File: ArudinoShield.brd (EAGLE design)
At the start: 53.3 x 61.9 mm, 21 parts, among them IC1 L298

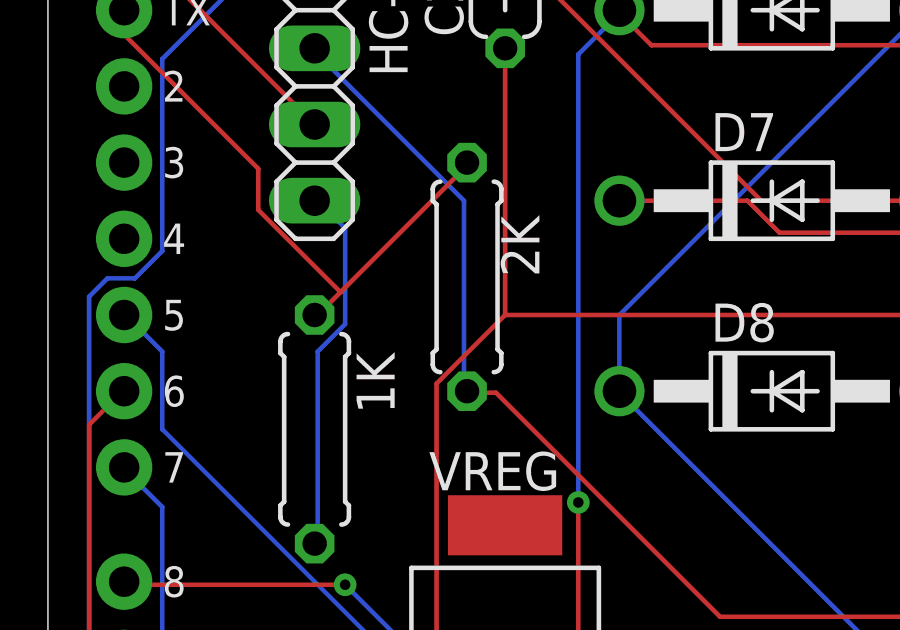
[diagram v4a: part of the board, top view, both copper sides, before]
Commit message: added values, updated gitignore for eagle files
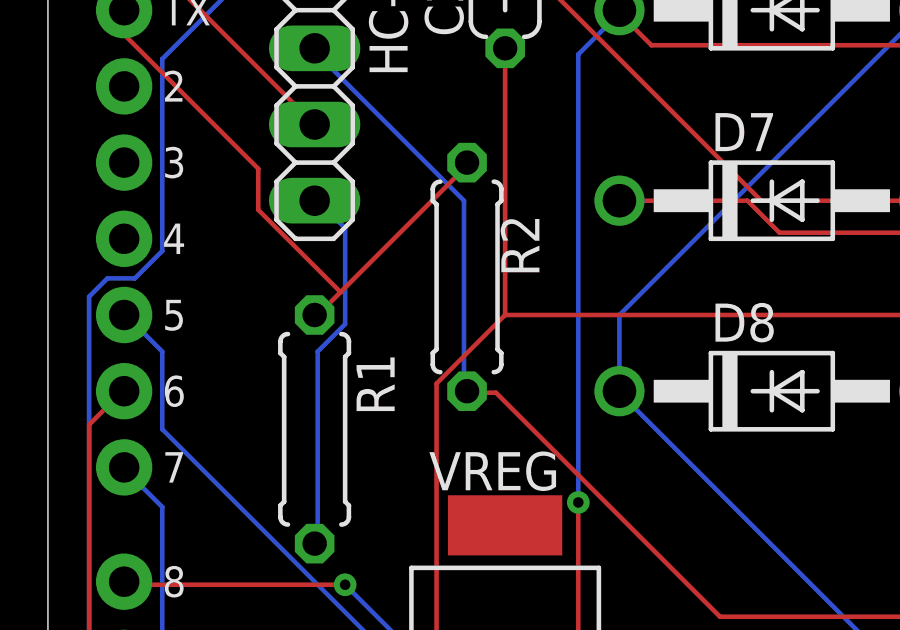
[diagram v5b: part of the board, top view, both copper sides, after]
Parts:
- C1, C2: value (none) -> 220uF/35V
- R1, R3: value (none) -> 1k
- R2: value (none) -> 2K
- renumbered 1K to R1, 2K to R2
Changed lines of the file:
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@@
 <attribute name="VALUE" x="40.005" y="73.66" size="1.27" layer="27" rot="R270"/>
 </element>
-<element name="1K" library="adafruit" package="0207/7" value="" x="43.18" y="57.15" smashed="yes" rot="R270">
+<element name="R1" library="adafruit" package="0207/7" value="1k" x="43.18" y="57.15" smashed="yes" rot="R270">
 <attribute name="NAME" x="44.577" y="59.69" size="1.27" layer="25" ratio="10" rot="R270"/>
 <attribute name="VALUE" x="42.6212" y="59.436" size="1.27" layer="27" ratio="10" rot="R270"/>
 </element>
-<element name="2K" library="adafruit" package="0207/7" value="" x="48.26" y="62.23" smashed="yes" rot="R90">
+<element name="R2" library="adafruit" package="0207/7" value="2K" x="48.26" y="62.23" smashed="yes" rot="R90">
 <attribute name="NAME" x="50.673" y="62.23" size="1.27" layer="25" ratio="10" rot="R90"/>
 <attribute name="VALUE" x="48.8188" y="59.944" size="1.27" layer="27" ratio="10" rot="R90"/>
@@
 <attribute name="VALUE" x="75.3031" y="28.5448" size="1.27" layer="27"/>
 </element>
-<element name="C1" library="rcl" library_urn="urn:adsk.eagle:library:334" package="C050-024X044" package3d_urn="urn:adsk.eagle:package:23643/1" value="" x="38.1" y="24.13" smashed="yes" rot="R90">
+<element name="C1" library="rcl" library_urn="urn:adsk.eagle:library:334" package="C050-024X044" package3d_urn="urn:adsk.eagle:package:23643/1" value="220uF/35V" x="38.1" y="24.13" smashed="yes" rot="R90">
 <attribute name="NAME" x="36.703" y="21.971" size="1.27" layer="25" ratio="10" rot="R90"/>
 <attribute name="POPULARITY" value="14" x="76.2" y="-34.29" size="1.778" layer="27" rot="R90" display="off"/>
@@
 <attribute name="VALUE" x="40.767" y="21.971" size="1.27" layer="27" ratio="10" rot="R90"/>
 </element>
-<element name="C2" library="rcl" library_urn="urn:adsk.eagle:library:334" package="C050-024X044" package3d_urn="urn:adsk.eagle:package:23643/1" value="" x="49.53" y="72.39" smashed="yes" rot="R90">
+<element name="C2" library="rcl" library_urn="urn:adsk.eagle:library:334" package="C050-024X044" package3d_urn="urn:adsk.eagle:package:23643/1" value="220uF/35V" x="49.53" y="72.39" smashed="yes" rot="R90">
 <attribute name="NAME" x="48.133" y="70.231" size="1.27" layer="25" ratio="10" rot="R90"/>
 <attribute name="POPULARITY" value="14" x="92.71" y="6.35" size="1.778" layer="27" rot="R90" display="off"/>
@@
 <attribute name="VALUE" x="52.197" y="70.231" size="1.27" layer="27" ratio="10" rot="R90"/>
 </element>
-<element name="R3" library="rcl" library_urn="urn:adsk.eagle:library:334" package="0207/10" package3d_urn="urn:adsk.eagle:package:23491/2" value="" x="43.18" y="44.45" smashed="yes" rot="R90">
+<element name="R3" library="rcl" library_urn="urn:adsk.eagle:library:334" package="0207/10" package3d_urn="urn:adsk.eagle:package:23491/2" value="1k" x="43.18" y="44.45" smashed="yes" rot="R90">
 <attribute name="NAME" x="41.656" y="41.402" size="1.27" layer="25" ratio="10" rot="R90"/>
 <attribute name="POPULARITY" value="36" x="91.44" y="-1.27" size="1.778" layer="27" rot="R90" display="off"/>
@@
 <contactref element="HC-05" pad="2"/>
 <contactref element="B1" pad="GND@0"/>
-<contactref element="2K" pad="1"/>
+<contactref element="R2" pad="1"/>
 <wire x1="48.1584" y1="64.77" x2="48.1584" y2="58.5216" width="0.1524" layer="16"/>
 <wire x1="43.1292" y1="69.7992" x2="48.1584" y2="64.77" width="0.1524" layer="16"/>
@@
 </signal>
 <signal name="N$11">
-<contactref element="1K" pad="1"/>
+<contactref element="R1" pad="1"/>
 <contactref element="B1" pad="TX"/>
-<contactref element="2K" pad="2"/>
+<contactref element="R2" pad="2"/>
 <wire x1="48.3108" y1="65.9892" x2="44.0436" y2="61.722" width="0.1524" layer="1"/>
 <wire x1="44.0436" y1="61.722" x2="43.2816" y2="60.96" width="0.1524" layer="1"/>
@@
 </signal>
 <signal name="N$14">
-<contactref element="1K" pad="2"/>
+<contactref element="R1" pad="2"/>
 <contactref element="HC-05" pad="4"/>
 <wire x1="43.2816" y1="59.7408" x2="43.2816" y2="53.34" width="0.1524" layer="16"/>

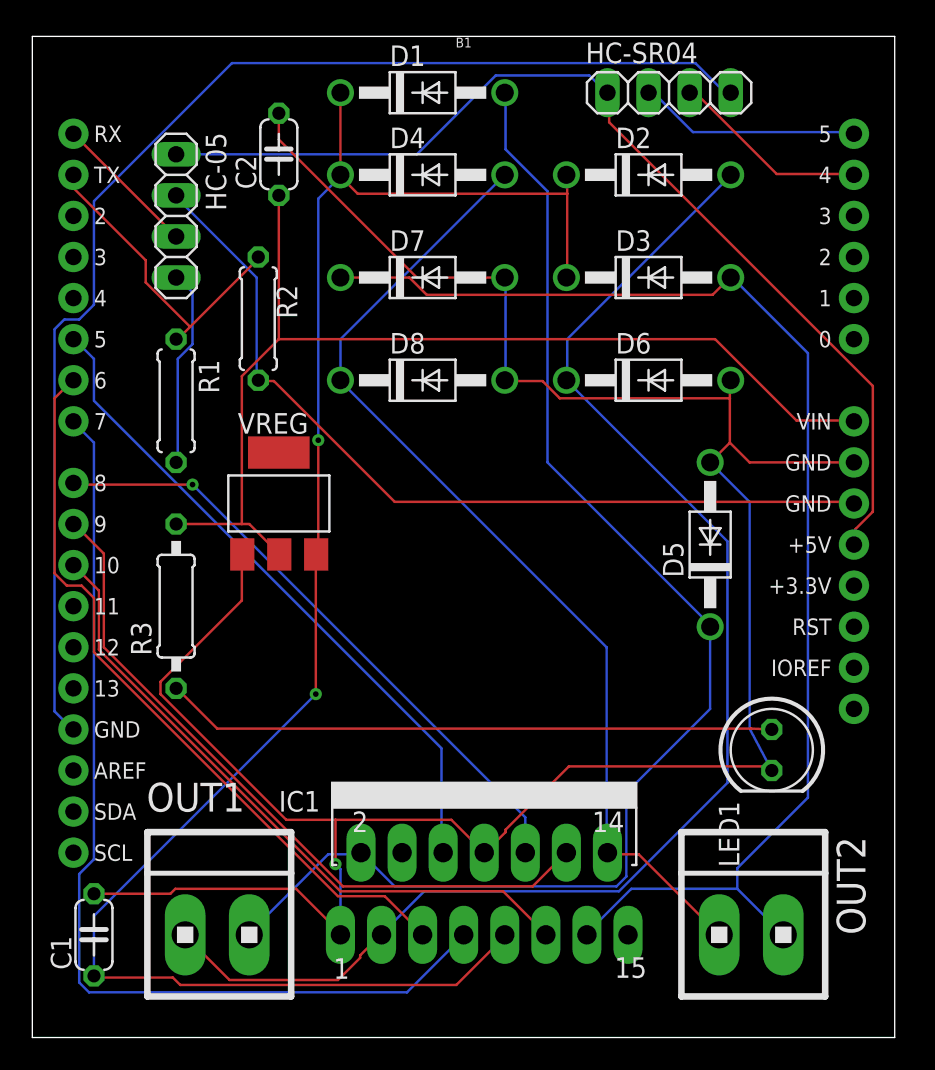
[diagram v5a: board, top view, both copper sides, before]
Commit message: updated schematic for proper pinout from L298 and added supply voltage terminal block
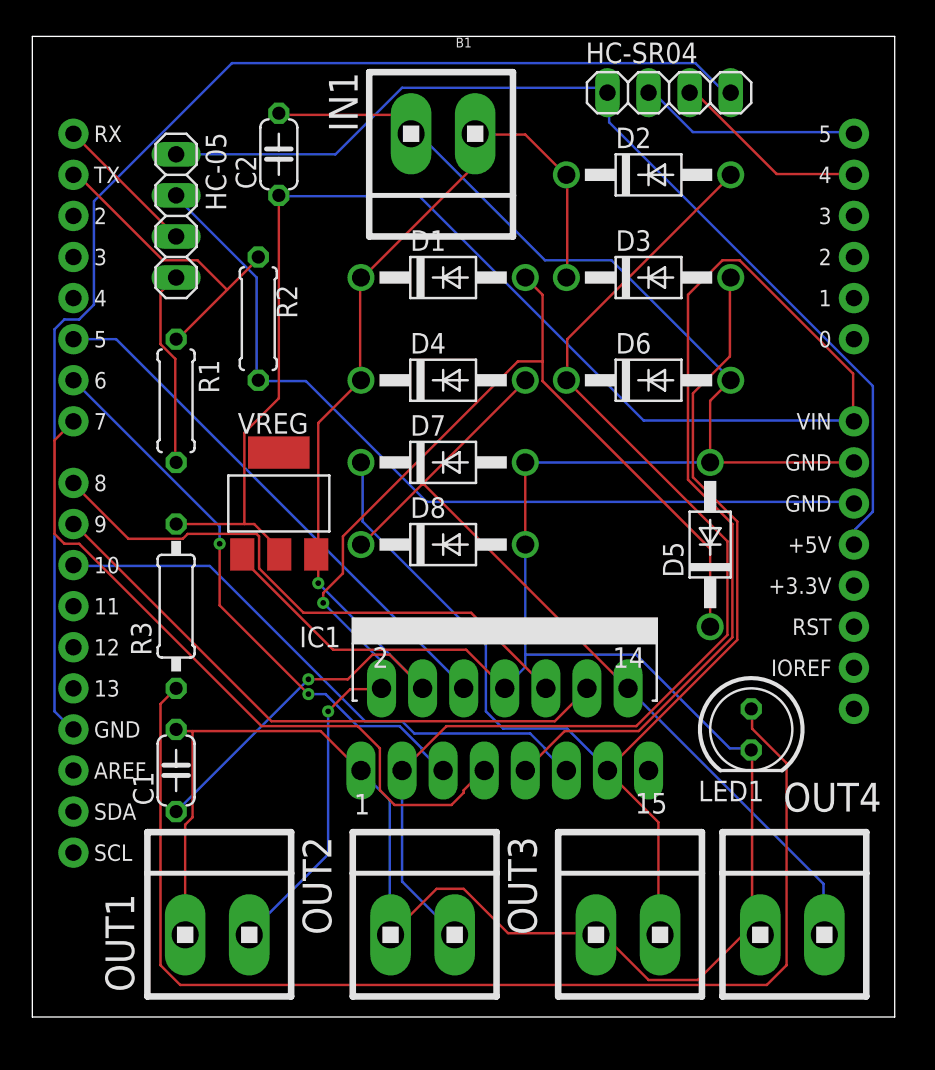
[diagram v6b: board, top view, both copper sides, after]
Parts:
- added IN1, OUT3, OUT4: (no value), con-amp:1X2MTA
- moved OUT2 20.3 mm to (58.4, 24.1)
- moved D4 12.8 mm to (59.7, 58.4)
- moved D1 11.5 mm to (59.7, 64.8)
- moved D7 11.5 mm to (59.7, 53.3)
- moved C1 11.4 mm to (43.2, 34.3)
- moved D8 10.2 mm to (59.7, 48.3)
- moved IC1 10.2 mm to (63.5, 41.9)
- moved LED1 1.80 mm to (78.7, 36.8)
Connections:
- removed net VS: IC1.4
- net N$16: now also OUT2.1; no longer OUT1.2
- net N$17: now also OUT3.1; no longer OUT2.1
- net N$18: now also OUT4.1; no longer OUT2.2
- net N$26: now also IC1.9
- net N$29: now also IN1.1, OUT1.2, OUT2.2, OUT3.2, OUT4.2
- net N$31: now also IC1.4, IN1.2; no longer IC1.9
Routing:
- net N$26: track 66.1 -> 125.4 mm
- net N$25: track 37.9 -> 74.0 mm
- net N$29: track 152.9 -> 187.4 mm, vias 1 -> 0
- net N$31: track 109.0 -> 74.5 mm
- net N$22: track 61.1 -> 43.4 mm
- net N$16: track 85.8 -> 71.8 mm
- net N$21: track 46.4 -> 35.8 mm, vias 0 -> 2
- net N$18: track 62.0 -> 52.6 mm
- net N$15: track 82.5 -> 74.3 mm, vias 0 -> 2
- net N$1: track 41.3 -> 33.1 mm
- net N$24: track 44.0 -> 37.7 mm
- net N$17: track 81.2 -> 75.4 mm
- net N$20: track 40.8 -> 35.8 mm
- net N$2: track 38.7 -> 35.9 mm, vias 1 -> 0
- net N$10: track 64.4 -> 63.8 mm
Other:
- board size 53.3 x 61.9 mm -> 53.3 x 60.6 mm

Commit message: updated schematic and board
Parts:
- added 9G: (no value), pinhead:1X03
- moved R1 11.4 mm to (43.2, 45.7)
- moved HC-05 10.2 mm to (43.2, 58.4)
- moved R3 8.98 mm to (49.5, 38.1)
- moved C1 1.27 mm to (43.2, 35.6)
- renumbered IN1 to VIN
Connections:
- net N$1 renamed ENA
- net N$15 renamed OUT1
- net N$16 renamed OUT2
- net N$17 renamed OUT3
- net N$18 renamed OUT4
- net N$2 renamed IN3
- net N$20 renamed ENB
- net N$21 renamed IN1
- net N$22 renamed IN2
- net N$24 renamed IN4
- net N$31 renamed VIN
- net N$7 renamed ECHO
- net N$8 renamed TRIG
- removed net N$26: B1.VIN, C2.1, IC1.9, R3.2, VREG.2
- removed net N$29: B1.GND@1, C1.2, C2.2, D5.A, D6.A, D7.A, D8.A, IC1.1, IC1.8, LED1.K, OUT1.2, OUT2.2, OUT3.2, OUT4.2, VIN.1, VREG.1
- removed net N$9: B1.GND@2, HC-SR04.4
- new net +5V: 9G.2, B1.VIN, C2.1, IC1.9, R3.2, VREG.2
- new net 9GPWM: 9G.1, B1.D11
- new net GND: 9G.3, B1.GND@1, C1.2, C2.2, D5.A, D6.A, D7.A, D8.A, HC-SR04.4, IC1.1, IC1.15, IC1.8, LED1.K, OUT1.2, OUT2.2, OUT3.2, OUT4.2, VIN.1, VREG.1
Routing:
- net GND: track 0.00 -> 215.0 mm
- net N$29: track 187.4 -> 0.00 mm
- net N$26: track 125.4 -> 0.00 mm
- net +5V: track 0.00 -> 109.1 mm, vias 0 -> 1
- net N$9: track 78.4 -> 0.00 mm
- net N$25: track 74.0 -> 31.3 mm
- net 9GPWM: track 0.00 -> 26.8 mm
- net ENB: track 35.8 -> 60.3 mm
- net IN2: track 43.4 -> 67.8 mm
- net OUT3: track 75.4 -> 98.1 mm
- net N$11: track 19.8 -> 37.9 mm
- net ENA: track 33.1 -> 50.3 mm
- net IN4: track 37.7 -> 54.6 mm, vias 0 -> 1
- net N$12: track 8.98 -> 19.2 mm
- net IN1: track 35.8 -> 44.0 mm
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
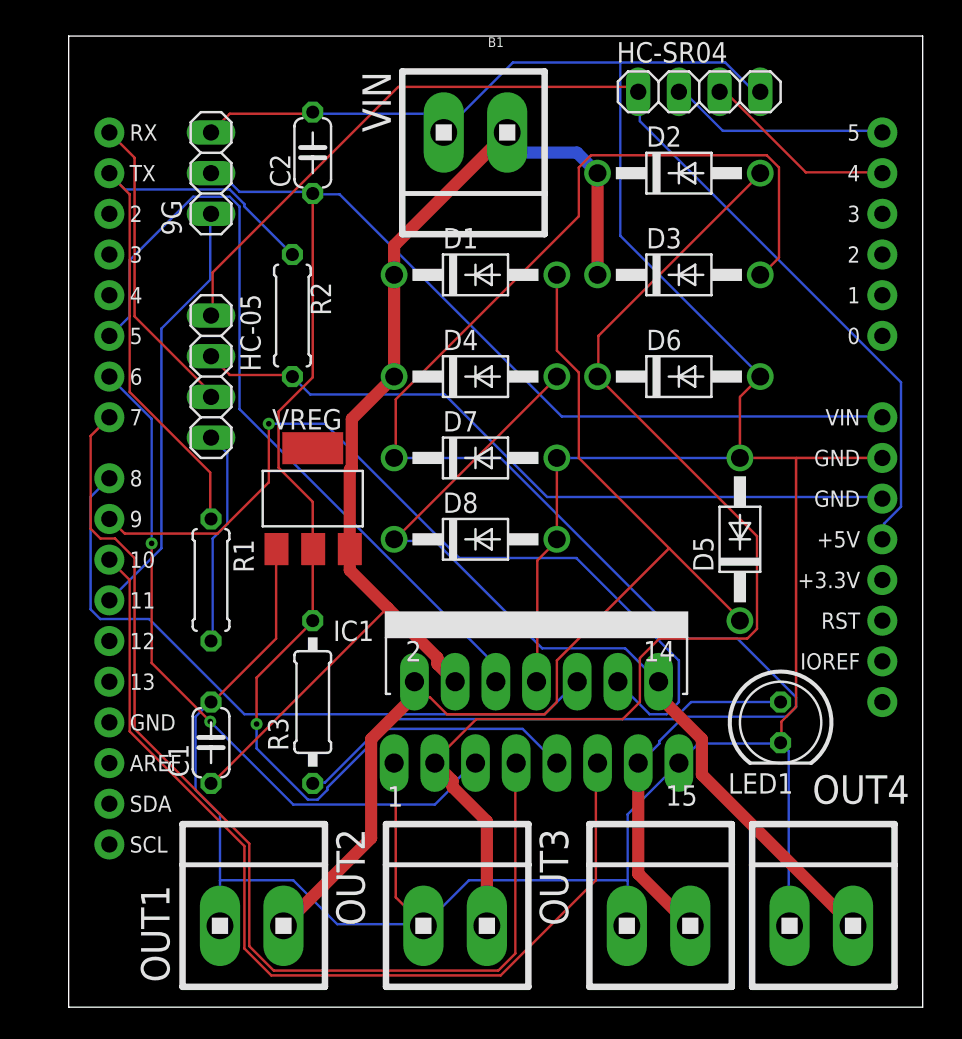
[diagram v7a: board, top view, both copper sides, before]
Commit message: updated power trace size
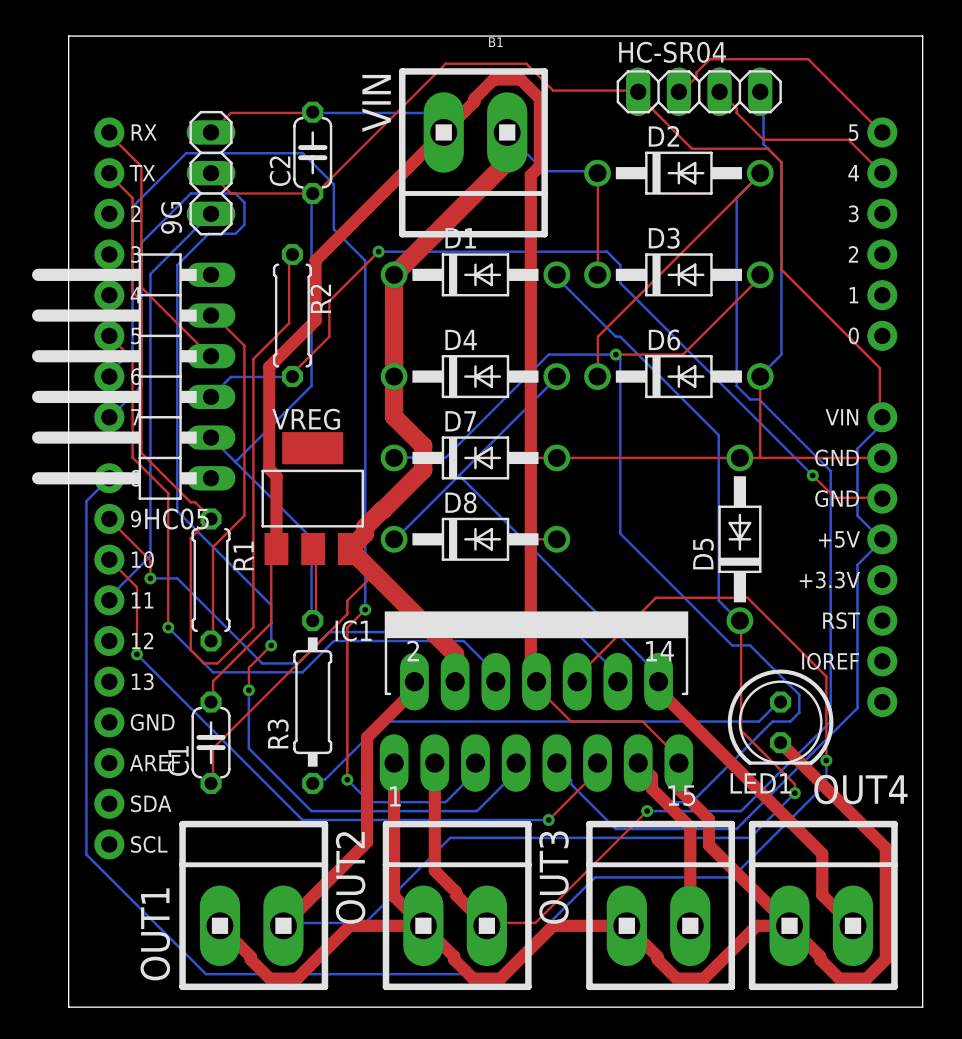
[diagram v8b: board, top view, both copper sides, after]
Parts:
- removed HC-05: (no value), pinhead:1X04
- added HC05: (no value), pinhead:1X06/90
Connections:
- removed net N$10: B1.5V, HC-05.1, HC-SR04.1
- net +5V: now also B1.5V, HC-SR04.1, HC05.2
- net N$12: now also HC05.4; no longer HC-05.3
- net N$13: now also HC05.3; no longer HC-05.2
- net N$14: now also HC05.5; no longer HC-05.4
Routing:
- net N$10: track 69.5 -> 0.00 mm
- net IN3: track 42.6 -> 104.9 mm, vias 0 -> 1
- net GND: track 215.0 -> 253.5 mm
- net +5V: track 109.1 -> 142.4 mm, vias 1 -> 0
- net IN1: track 44.0 -> 74.3 mm
- net OUT1: track 67.8 -> 92.7 mm, vias 0 -> 1
- net N$11: track 37.9 -> 62.6 mm
- net OUT2: track 73.5 -> 92.7 mm, vias 0 -> 1
- net ENB: track 60.3 -> 41.5 mm, vias 0 -> 2
- net OUT3: track 98.1 -> 80.6 mm, vias 0 -> 1
- net IN4: track 54.6 -> 38.6 mm
- net IN2: track 67.8 -> 79.4 mm, vias 0 -> 2
- net N$14: track 13.6 -> 22.3 mm
- net N$13: track 45.6 -> 54.1 mm, vias 0 -> 2
- net ENA: track 50.3 -> 43.5 mm, vias 0 -> 1
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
